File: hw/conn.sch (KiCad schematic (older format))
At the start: 8 parts, among them SW1 SW_DIP_x04

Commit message: hw: add servo conn
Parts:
- XP10: footprint (none) -> hat:SERVO4
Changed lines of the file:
@@
 F 0 "XP10" H 3600 6200 60  0000 L CNN
 F 1 "SERVO" H 3600 5550 60  0000 L CNN
-F 2 "" H 3650 5900 60  0001 C CNN
+F 2 "hat:SERVO4" H 3650 5900 60  0001 C CNN
 F 3 "" H 3650 5900 60  0001 C CNN
 	1    3700 5900
@@
 F 0 "XP10" H 4250 6200 60  0000 L CNN
 F 1 "SERVO" H 4477 5847 60  0001 L CNN
-F 2 "" H 4300 5900 60  0001 C CNN
+F 2 "hat:SERVO4" H 4300 5900 60  0001 C CNN
 F 3 "" H 4300 5900 60  0001 C CNN
 	2    4350 5900
@@
 F 0 "XP10" H 4900 6200 60  0000 L CNN
 F 1 "SERVO" H 5127 5847 60  0001 L CNN
-F 2 "" H 4950 5900 60  0001 C CNN
+F 2 "hat:SERVO4" H 4950 5900 60  0001 C CNN
 F 3 "" H 4950 5900 60  0001 C CNN
 	3    5000 5900

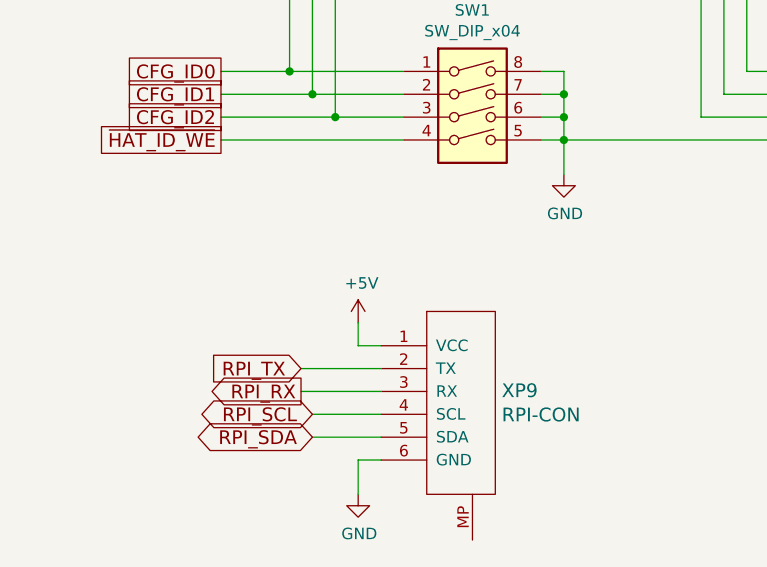
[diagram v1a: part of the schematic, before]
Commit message: hw: add battery input connector
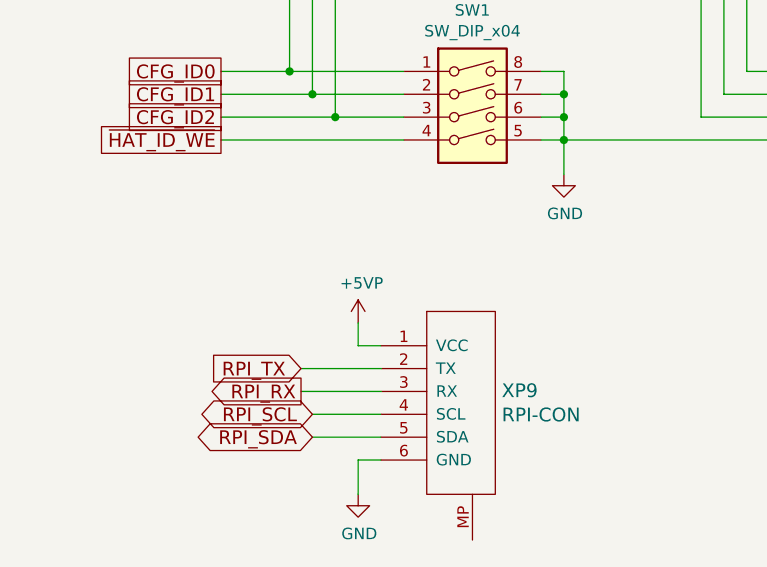
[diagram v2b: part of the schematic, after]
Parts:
- XP14: footprint (none) -> hat:XT30
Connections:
- net +5V: no longer XP9.1 (VCC)
- new net +5VP: XP9.1 (VCC)
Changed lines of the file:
@@
-	1    0    0    -1
-$EndComp
-$Comp
-L power:+5V #PWR050
-U 1 1 5AE1FAB8
-P 3750 4050
-F 0 "#PWR050" H 3750 3900 50  0001 C CNN
-F 1 "+5V" H 3765 4223 50  0000 C CNN
-F 2 "" H 3750 4050 50  0001 C CNN
-F 3 "" H 3750 4050 50  0001 C CNN
-	1    3750 4050
 	1    0    0    -1
 $EndComp
@@
 F 0 "XP14" H 5080 8642 50  0000 L CNN
 F 1 "BATT" H 5080 8551 50  0000 L CNN
-F 2 "" H 5000 8650 50  0001 C CNN
+F 2 "hat:XT30" H 5000 8650 50  0001 C CNN
 F 3 "~" H 5000 8650 50  0001 C CNN
 	1    5000 8650
@@
 	1    0    0    -1
 $EndComp
+$Comp
+L power:+5VP #PWR?
+U 1 1 5ACF44C1
+P 3750 4050
+F 0 "#PWR?" H 3750 3900 50  0001 C CNN
+F 1 "+5VP" H 3765 4223 50  0000 C CNN
+F 2 "" H 3750 4050 50  0001 C CNN
+F 3 "" H 3750 4050 50  0001 C CNN
+	1    3750 4050
+	1    0    0    -1
+$EndComp

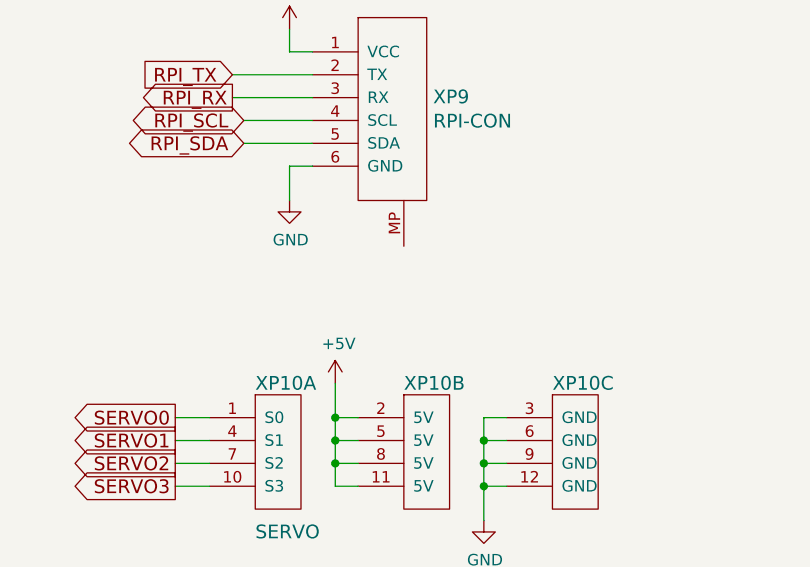
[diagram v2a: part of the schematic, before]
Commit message: hw: connect GH mount points with GND, add 3V battery
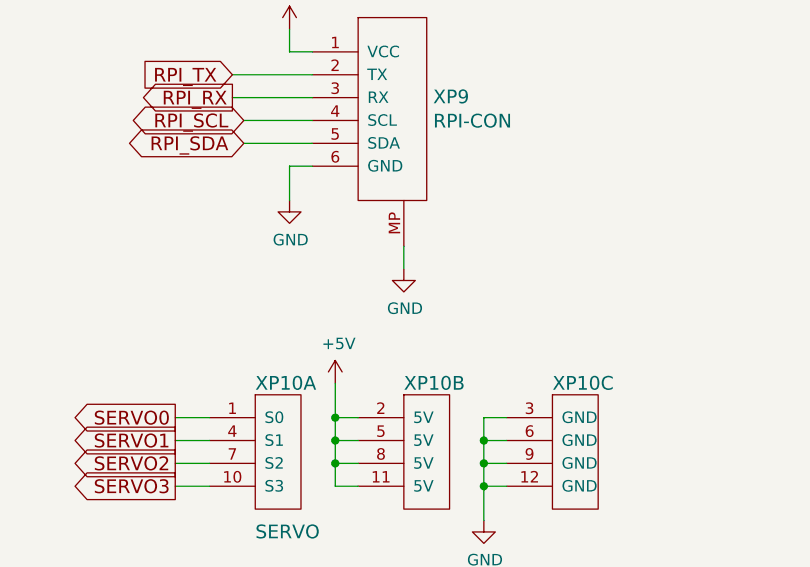
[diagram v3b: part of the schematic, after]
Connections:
- net GND: now also XP9.MP
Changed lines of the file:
@@
 $EndComp
 $Comp
-L power:+5VP #PWR?
+L power:+5VP #PWR0101
 U 1 1 5ACF44C1
 P 3750 4050
-F 0 "#PWR?" H 3750 3900 50  0001 C CNN
+F 0 "#PWR0101" H 3750 3900 50  0001 C CNN
 F 1 "+5VP" H 3765 4223 50  0000 C CNN
 F 2 "" H 3750 4050 50  0001 C CNN
@@
 	1    0    0    -1
 $EndComp
+$Comp
+L power:GND #PWR?
+U 1 1 5ACF6FA9
+P 4250 5100
+F 0 "#PWR?" H 4250 4850 50  0001 C CNN
+F 1 "GND" H 4255 4927 50  0000 C CNN
+F 2 "" H 4250 5100 50  0001 C CNN
+F 3 "" H 4250 5100 50  0001 C CNN
+	1    4250 5100
+	1    0    0    -1
+$EndComp
+Wire Wire Line
+	4250 5000 4250 5100
 $EndSCHEMATC

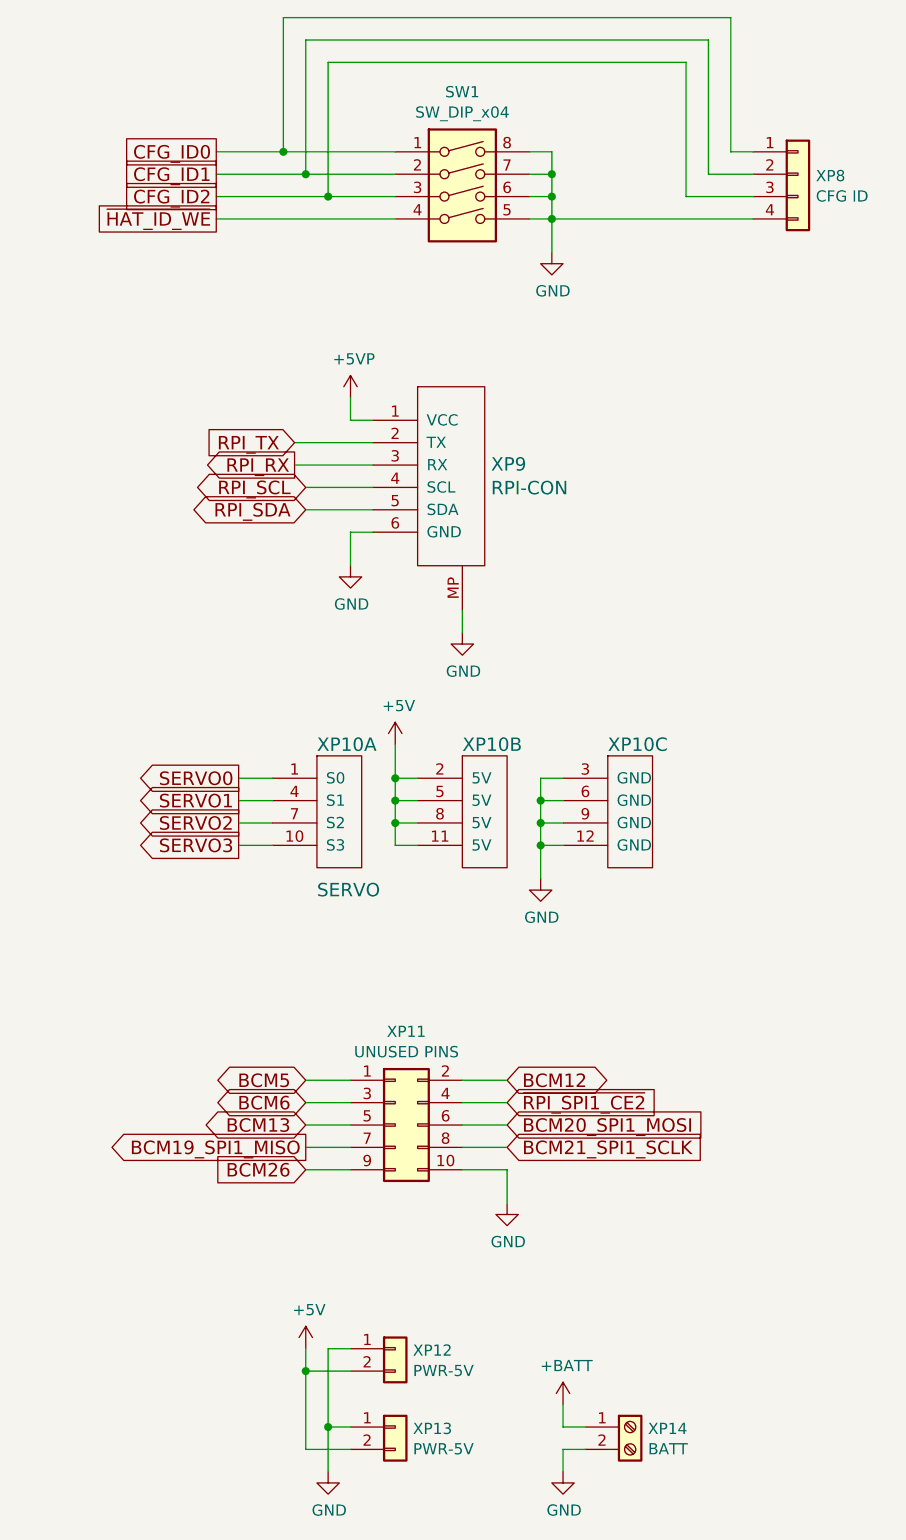
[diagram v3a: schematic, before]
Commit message: hw: remove header with unused rpi gpio's, more net labels
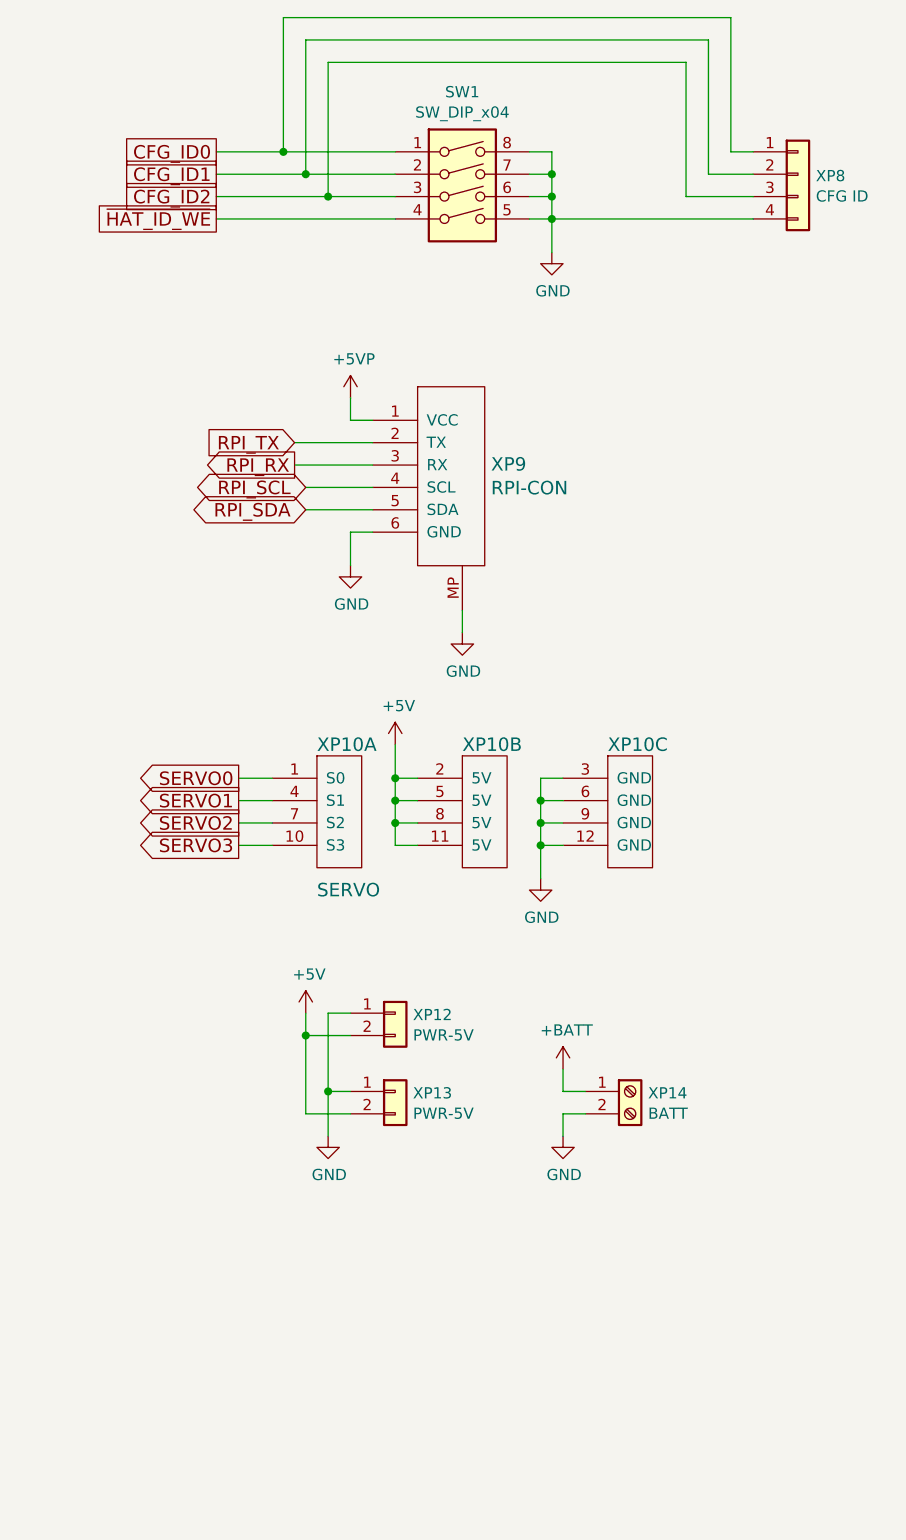
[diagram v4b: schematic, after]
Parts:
- removed XP11: UNUSED PINS, Connector_PinSocket_2.00mm:PinSocket_2x05_P2.00mm_Vertical, symbol Connector_Generic:Conn_02x05_Odd_Even
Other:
- moved on the sheet: XP12, XP13, XP14
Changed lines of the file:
@@
 Text GLabel 3500 4350 0    60   Output ~ 0
 RPI_RX
-Text GLabel 4450 7300 2    60   Input ~ 0
-BCM20_SPI1_MOSI
-Text GLabel 4450 7400 2    60   Input ~ 0
-BCM21_SPI1_SCLK
-Text GLabel 4450 7200 2    60   Input ~ 0
-~RPI_SPI1_CE2
-Text GLabel 4450 7100 2    60   BiDi ~ 0
-BCM12
 Text GLabel 3550 4450 0    60   BiDi ~ 0
 RPI_SCL
 Text GLabel 3550 4550 0    60   BiDi ~ 0
 RPI_SDA
-Text GLabel 3550 7400 0    60   Output ~ 0
-BCM19_SPI1_MISO
-Text GLabel 3550 7500 0    60   Input ~ 0
-BCM26
-Text GLabel 3550 7300 0    60   BiDi ~ 0
-BCM13
-Text GLabel 3550 7100 0    60   BiDi ~ 0
-BCM5
-Text GLabel 3550 7200 0    60   BiDi ~ 0
-BCM6
 Wire Wire Line
 	3550 4450 3850 4450
@@
 	3750 4650 3750 4800
 $Comp
-L Connector_Generic:Conn_02x05_Odd_Even XP11
-U 1 1 5AE27376
-P 3950 7300
-F 0 "XP11" H 4000 7717 50  0000 C CNN
-F 1 "UNUSED PINS" H 4000 7626 50  0000 C CNN
-F 2 "Connector_PinSocket_2.00mm:PinSocket_2x05_P2.00mm_Vertical" H 3950 7300 50  0001 C CNN
-F 3 "~" H 3950 7300 50  0001 C CNN
-	1    3950 7300
-	1    0    0    -1
-$EndComp
-$Comp
-L power:GND #PWR054
-U 1 1 5AE2781B
-P 4450 7650
-F 0 "#PWR054" H 4450 7400 50  0001 C CNN
-F 1 "GND" H 4455 7477 50  0000 C CNN
-F 2 "" H 4450 7650 50  0001 C CNN
-F 3 "" H 4450 7650 50  0001 C CNN
-	1    4450 7650
-	1    0    0    -1
-$EndComp
-Wire Wire Line
-	3550 7100 3750 7100
-Wire Wire Line
-	3550 7200 3750 7200
-Wire Wire Line
-	3550 7300 3750 7300
-Wire Wire Line
-	3550 7400 3750 7400
-Wire Wire Line
-	3550 7500 3750 7500
-Wire Wire Line
-	4250 7100 4450 7100
-Wire Wire Line
-	4450 7200 4250 7200
-Wire Wire Line
-	4450 7300 4250 7300
-Wire Wire Line
-	4450 7400 4250 7400
-Wire Wire Line
-	4250 7500 4450 7500
-Wire Wire Line
-	4450 7500 4450 7650
-$Comp
 L Connector_Generic:Conn_01x02 XP12
 U 1 1 5ADAC8B3
-P 3950 8300
-F 0 "XP12" H 4029 8292 50  0000 L CNN
-F 1 "PWR-5V" H 4029 8201 50  0000 L CNN
-F 2 "Connector_JST:JST_PH_B2B-PH-K_1x02_P2.00mm_Vertical" H 3950 8300 50  0001 C CNN
-F 3 "~" H 3950 8300 50  0001 C CNN
-	1    3950 8300
+P 3950 6800
+F 0 "XP12" H 4029 6792 50  0000 L CNN
+F 1 "PWR-5V" H 4029 6701 50  0000 L CNN
+F 2 "Connector_JST:JST_PH_B2B-PH-K_1x02_P2.00mm_Vertical" H 3950 6800 50  0001 C CNN
+F 3 "~" H 3950 6800 50  0001 C CNN
+	1    3950 6800
 	1    0    0    -1
 $EndComp
@@
 L Connector_Generic:Conn_01x02 XP13
 U 1 1 5ADACAD0
-P 3950 8650
-F 0 "XP13" H 4029 8642 50  0000 L CNN
-F 1 "PWR-5V" H 4029 8551 50  0000 L CNN
-F 2 "Connector_JST:JST_PH_B2B-PH-K_1x02_P2.00mm_Vertical" H 3950 8650 50  0001 C CNN
-F 3 "~" H 3950 8650 50  0001 C CNN
-	1    3950 8650
+P 3950 7150
+F 0 "XP13" H 4029 7142 50  0000 L CNN
+F 1 "PWR-5V" H 4029 7051 50  0000 L CNN
+F 2 "Connector_JST:JST_PH_B2B-PH-K_1x02_P2.00mm_Vertical" H 3950 7150 50  0001 C CNN
+F 3 "~" H 3950 7150 50  0001 C CNN
+	1    3950 7150
 	1    0    0    -1
 $EndComp
@@
 L power:GND #PWR057
 U 1 1 5ADAE6E2
-P 3650 8850
-F 0 "#PWR057" H 3650 8600 50  0001 C CNN
-F 1 "GND" H 3655 8677 50  0000 C CNN
-F 2 "" H 3650 8850 50  0001 C CNN
-F 3 "" H 3650 8850 50  0001 C CNN
-	1    3650 8850
+P 3650 7350
+F 0 "#PWR057" H 3650 7100 50  0001 C CNN
+F 1 "GND" H 3655 7177 50  0000 C CNN
+F 2 "" H 3650 7350 50  0001 C CNN
+F 3 "" H 3650 7350 50  0001 C CNN
+	1    3650 7350
 	1    0    0    -1
 $EndComp
@@
 L power:+5V #PWR055
 U 1 1 5ADAEA7B
-P 3550 8300
-F 0 "#PWR055" H 3550 8150 50  0001 C CNN
-F 1 "+5V" H 3565 8473 50  0000 C CNN
-F 2 "" H 3550 8300 50  0001 C CNN
-F 3 "" H 3550 8300 50  0001 C CNN
-	1    3550 8300
-	1    0    0    -1
-$EndComp
-Wire Wire Line
-	3750 8300 3650 8300
-Wire Wire Line
-	3650 8300 3650 8650
-Wire Wire Line
-	3650 8650 3750 8650
-Connection ~ 3650 8650
-Wire Wire Line
-	3650 8650 3650 8850
-Wire Wire Line
-	3750 8750 3550 8750
-Wire Wire Line
-	3550 8750 3550 8400
-Wire Wire Line
-	3750 8400 3550 8400
-Connection ~ 3550 8400
-Wire Wire Line
-	3550 8400 3550 8300
+P 3550 6800
+F 0 "#PWR055" H 3550 6650 50  0001 C CNN
+F 1 "+5V" H 3565 6973 50  0000 C CNN
+F 2 "" H 3550 6800 50  0001 C CNN
+F 3 "" H 3550 6800 50  0001 C CNN
+	1    3550 6800
+	1    0    0    -1
+$EndComp
+Wire Wire Line
+	3750 6800 3650 6800
+Wire Wire Line
+	3650 6800 3650 7150
+Wire Wire Line
+	3650 7150 3750 7150
+Connection ~ 3650 7150
+Wire Wire Line
+	3650 7150 3650 7350
+Wire Wire Line
+	3750 7250 3550 7250
+Wire Wire Line
+	3550 7250 3550 6900
+Wire Wire Line
+	3750 6900 3550 6900
+Connection ~ 3550 6900
+Wire Wire Line
+	3550 6900 3550 6800
 $Comp
 L Connector_Specialized:Screw_Terminal_01x02 XP14
 U 1 1 5ADC296E
-P 5000 8650
-F 0 "XP14" H 5080 8642 50  0000 L CNN
-F 1 "BATT" H 5080 8551 50  0000 L CNN
-F 2 "hat:XT30" H 5000 8650 50  0001 C CNN
-F 3 "~" H 5000 8650 50  0001 C CNN
-	1    5000 8650
+P 5000 7150
+F 0 "XP14" H 5080 7142 50  0000 L CNN
+F 1 "BATT" H 5080 7051 50  0000 L CNN
+F 2 "hat:XT30" H 5000 7150 50  0001 C CNN
+F 3 "~" H 5000 7150 50  0001 C CNN
+	1    5000 7150
 	1    0    0    -1
 $EndComp
@@
 L power:GND #PWR058
 U 1 1 5ADC2D33
-P 4700 8850
-F 0 "#PWR058" H 4700 8600 50  0001 C CNN
-F 1 "GND" H 4705 8677 50  0000 C CNN
-F 2 "" H 4700 8850 50  0001 C CNN
-F 3 "" H 4700 8850 50  0001 C CNN
-	1    4700 8850
+P 4700 7350
+F 0 "#PWR058" H 4700 7100 50  0001 C CNN
+F 1 "GND" H 4705 7177 50  0000 C CNN
+F 2 "" H 4700 7350 50  0001 C CNN
+F 3 "" H 4700 7350 50  0001 C CNN
+	1    4700 7350
 	1    0    0    -1
 $EndComp
@@
 L power:+BATT #PWR056
 U 1 1 5ADC2DB8
-P 4700 8550
-F 0 "#PWR056" H 4700 8400 50  0001 C CNN
-F 1 "+BATT" H 4715 8723 50  0000 C CNN
-F 2 "" H 4700 8550 50  0001 C CNN
-F 3 "" H 4700 8550 50  0001 C CNN
-	1    4700 8550
-	1    0    0    -1
-$EndComp
-Wire Wire Line
-	4800 8650 4700 8650
-Wire Wire Line
-	4700 8650 4700 8550
-Wire Wire Line
-	4800 8750 4700 8750
-Wire Wire Line
-	4700 8750 4700 8850
+P 4700 7050
+F 0 "#PWR056" H 4700 6900 50  0001 C CNN
+F 1 "+BATT" H 4715 7223 50  0000 C CNN
+F 2 "" H 4700 7050 50  0001 C CNN
+F 3 "" H 4700 7050 50  0001 C CNN
+	1    4700 7050
+	1    0    0    -1
+$EndComp
+Wire Wire Line
+	4800 7150 4700 7150
+Wire Wire Line
+	4700 7150 4700 7050
+Wire Wire Line
+	4800 7250 4700 7250
+Wire Wire Line
+	4700 7250 4700 7350
 $Comp
 L dronecode-conn:DC-GPS XP9
@@
 $EndComp
 $Comp
-L power:GND #PWR?
+L power:GND #PWR0106
 U 1 1 5ACF6FA9
 P 4250 5100
-F 0 "#PWR?" H 4250 4850 50  0001 C CNN
+F 0 "#PWR0106" H 4250 4850 50  0001 C CNN
 F 1 "GND" H 4255 4927 50  0000 C CNN
 F 2 "" H 4250 5100 50  0001 C CNN
